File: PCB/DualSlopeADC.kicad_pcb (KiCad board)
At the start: 2 copper layers, 47 x 71.9 mm, 37 parts, among them J2 Conn_01x02_Pin, J3 Conn_01x02_Pin, J5 Conn_01x02_Pin, J6 Conn_01x02_Pin, J7 Conn_01x02_Pin, J8 Conn_01x02_Pin, J9 Conn_01x02_Pin, U1 CH32V003FxPx, U2 ADR4533, U3 AD8605ARTZ-R2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

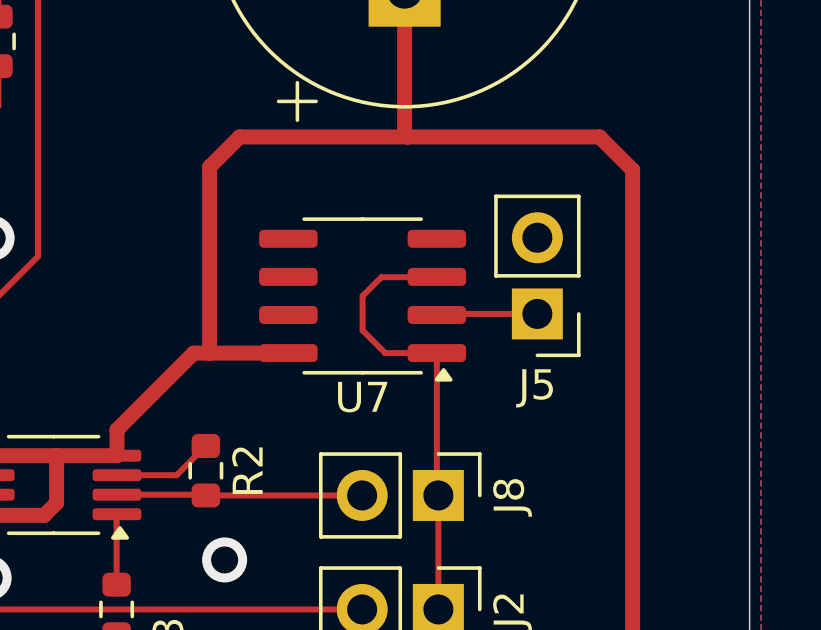
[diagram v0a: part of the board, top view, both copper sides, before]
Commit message: Fehler in pCB behoben durch OP
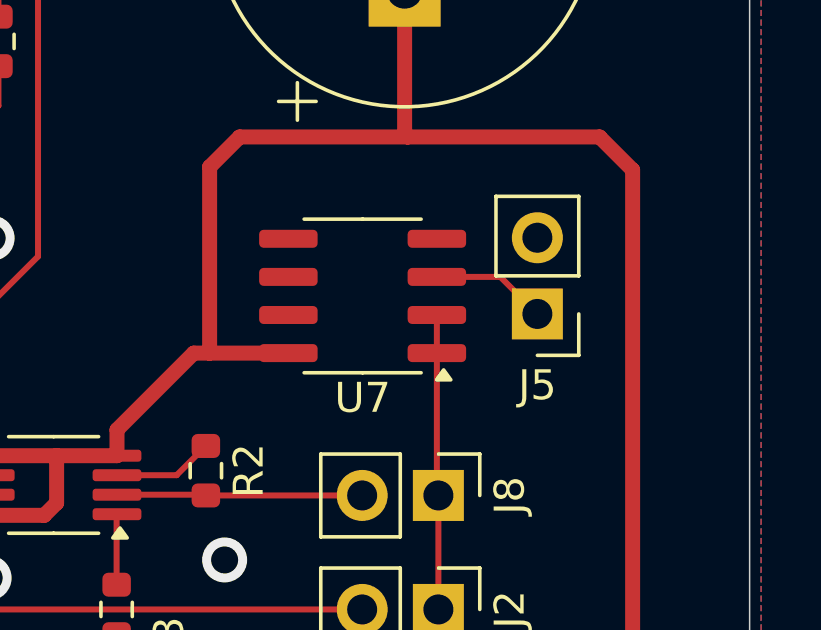
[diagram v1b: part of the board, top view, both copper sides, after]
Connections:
- U7 pad 2: Vin -> Net-(J2-Pin_1)
- U7 pad 3: Net-(J2-Pin_1) -> Vin
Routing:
- net Net-(J2-Pin_1): track 15.2 -> 9.89 mm
- net Vin: track 3.41 -> 3.93 mm
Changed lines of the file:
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@@
 			(layers "F.Cu" "F.Mask" "F.Paste")
 			(roundrect_rratio 0.25)
-			(net 6 "Vin")
+			(net 36 "Net-(J2-Pin_1)")
 			(pinfunction "-")
 			(pintype "input")
@@
 			(layers "F.Cu" "F.Mask" "F.Paste")
 			(roundrect_rratio 0.25)
-			(net 36 "Net-(J2-Pin_1)")
+			(net 6 "Vin")
 			(pinfunction "+")
 			(pintype "input")
@@
 	)
 	(segment
-		(start 153.91 103.7)
-		(end 153.875 103.735)
+		(start 155.99 102.465)
+		(end 153.875 102.465)
 		(width 0.2)
 		(layer "F.Cu")
@@
 	(segment
 		(start 157.225 103.7)
-		(end 153.91 103.7)
+		(end 155.99 102.465)
+		(width 0.2)
+		(layer "F.Cu")
+		(net 6)
+	)
+	(segment
+		(start 153.865 102.475)
+		(end 153.875 102.465)
 		(width 0.2)
 		(layer "F.Cu")
@@
 	)
 	(segment
+		(start 153.91 103.7)
+		(end 153.875 103.735)
+		(width 0.2)
+		(layer "F.Cu")
+		(net 36)
+	)
+	(segment
 		(start 153.875 109.7)
 		(end 153.925 109.75)
@@
 	)
 	(segment
-		(start 151.4 104.25)
-		(end 151.4 103.1)
-		(width 0.2)
-		(layer "F.Cu")
-		(net 36)
-	)
-	(segment
-		(start 152.025 102.475)
-		(end 153.865 102.475)
-		(width 0.2)
-		(layer "F.Cu")
-		(net 36)
-	)
-	(segment
-		(start 153.875 105.005)
-		(end 152.155 105.005)
-		(width 0.2)
-		(layer "F.Cu")
-		(net 36)
-	)
-	(segment
-		(start 151.4 103.1)
-		(end 152.025 102.475)
-		(width 0.2)
-		(layer "F.Cu")
-		(net 36)
-	)
-	(segment
 		(start 153.875 105.005)
 		(end 153.875 109.7)
@@
 	)
 	(segment
-		(start 153.865 102.475)
-		(end 153.875 102.465)
-		(width 0.2)
-		(layer "F.Cu")
-		(net 36)
-	)
-	(segment
 		(start 153.925 113.55)
 		(end 153.925 109.75)
@@
 	)
 	(segment
-		(start 152.155 105.005)
-		(end 151.4 104.25)
-		(width 0.2)
-		(layer "F.Cu")
+		(start 153.875 105.005)
+		(end 153.875 103.735)
+		(width 0.2)
+		(layer "F.Cu")

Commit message: visulle sachen
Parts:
- moved ? 55.0 mm to (107.8, 73.3), turned to 90 degrees (x3)
- moved ? 55.0 mm to (107.8, 114.3), turned to 90 degrees (x3)
- moved ? 54.9 mm to (173.8, 114.3), turned to 90 degrees (x3)
- moved ? 54.9 mm to (173.8, 73.3), turned to 90 degrees (x3)
- moved J3 43.1 mm to (169.2, 82.7), turned to 180 degrees
- moved J9 40.4 mm to (166.9, 105.5), turned to 0 degrees
- moved C3 40.0 mm to (168.9, 97.1), turned to 0 degrees
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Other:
- board size 47 x 71.9 mm -> 71.9 x 47 mm
